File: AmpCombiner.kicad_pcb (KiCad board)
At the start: 2 copper layers, 64.1 x 34.3 mm, 22 parts, among them J1 AudioJack4, J2 AudioJack4, J3 AudioJack4, SW1 SW_SPDT, U1 TDA1517

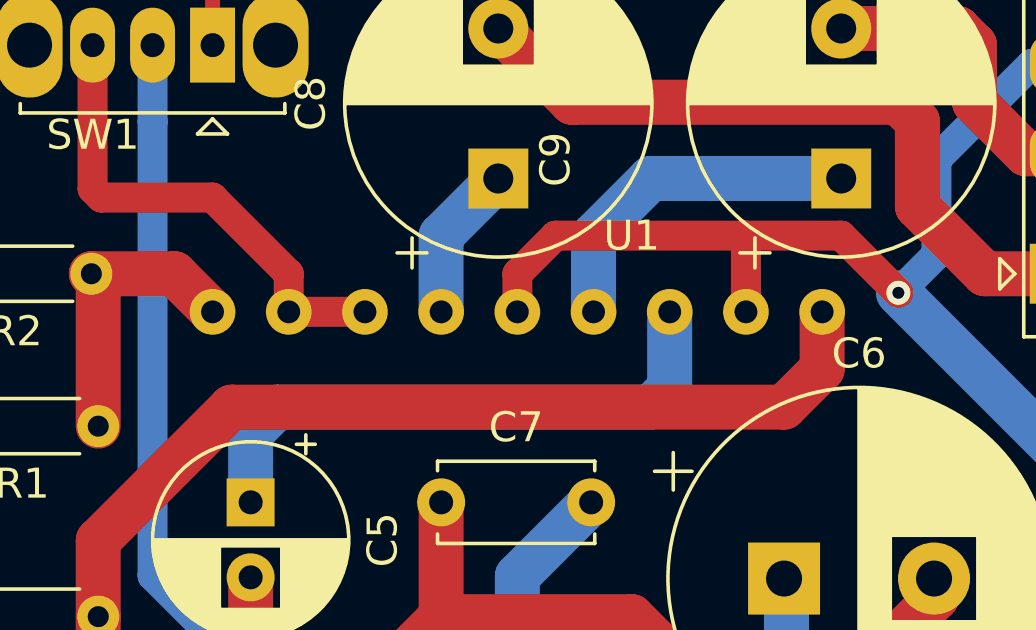
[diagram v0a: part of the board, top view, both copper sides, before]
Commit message: Update docs, standard footprint
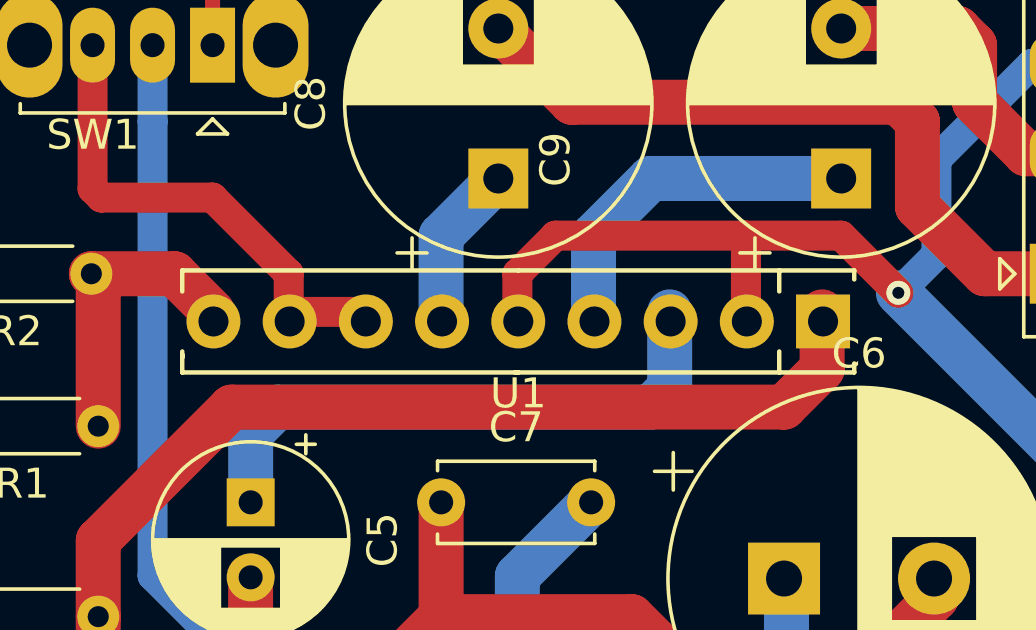
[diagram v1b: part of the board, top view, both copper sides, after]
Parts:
- U1: footprint KiLib:SOT110-1 -> Package_SIP:SIP9_Housing
- moved U1 7.81 mm to (172.8, 107.0)
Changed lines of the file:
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@@
   (general
     (thickness 1.6)
-    (drawings 5)
+    (drawings 7)
     (tracks 120)
     (zones 0)
@@
     (add_net "Net-(R3-Pad1)")
     (add_net "Net-(SW1-Pad3)")
+  )
+  (module Package_SIP:SIP9_Housing (layer F.Cu)
+    (at 172.75 107 180)
+    (descr SIP9)
+    (tags SIP9)
+    (fp_text reference U1 (at 10.16 -2.4) (layer F.SilkS)
+      (effects (font (size 1 1) (thickness 0.15)))
+    )
+    (fp_text value TDA1517 (at 10.16 2.5) (layer F.Fab)
+      (effects (font (size 1 1) (thickness 0.15)))
+    )
+    (fp_line (start 21.56 -1.9) (end -1.24 -2) (layer F.CrtYd) (width 0.05))
+    (fp_line (start 21.56 1.9) (end 21.56 -1.9) (layer F.CrtYd) (width 0.05))
+    (fp_line (start -1.24 2) (end 21.56 1.9) (layer F.CrtYd) (width 0.05))
+    (fp_line (start -1.24 -2) (end -1.24 2) (layer F.CrtYd) (width 0.05))
+    (fp_line (start 0.06 -1.6) (end 21.26 -1.6) (layer F.Fab) (width 0.1))
+    (fp_line (start -0.94 -0.6) (end 0.06 -1.6) (layer F.Fab) (width 0.1))
+    (fp_line (start -0.94 1.6) (end -0.94 -0.6) (layer F.Fab) (width 0.1))
+    (fp_line (start 21.26 1.6) (end -0.94 1.6) (layer F.Fab) (width 0.1))
+    (fp_line (start 21.26 -1.6) (end 21.26 1.6) (layer F.Fab) (width 0.1))
+    (fp_line (start 21.36 -1.7) (end 21.36 -1.1) (layer F.SilkS) (width 0.15))
+    (fp_line (start 10.16 -1.7) (end 21.36 -1.7) (layer F.SilkS) (width 0.15))
+    (fp_line (start -1.04 -1.7) (end -1.04 -1.4) (layer F.SilkS) (width 0.15))
+    (fp_line (start 10.26 -1.7) (end -1.04 -1.7) (layer F.SilkS) (width 0.15))
+    (fp_line (start 21.36 1.7) (end 21.36 1) (layer F.SilkS) (width 0.15))
+    (fp_line (start 10.16 1.7) (end 21.36 1.7) (layer F.SilkS) (width 0.15))
+    (fp_line (start 21.36 -1.2) (end 21.36 -1) (layer F.SilkS) (width 0.15))
+    (fp_line (start -1.04 1.7) (end -1.04 1.4) (layer F.SilkS) (width 0.15))
+    (fp_line (start 10.16 1.7) (end -1.04 1.7) (layer F.SilkS) (width 0.15))
+    (fp_line (start 1.46 -1.7) (end 1.46 -1) (layer F.SilkS) (width 0.15))
+    (fp_line (start 1.46 1.7) (end 1.46 1) (layer F.SilkS) (width 0.15))
+    (fp_text user %R (at 10.16 0) (layer F.Fab)
+      (effects (font (size 1 1) (thickness 0.15)))
+    )
+    (pad 9 thru_hole circle (at 20.32 0 270) (size 1.8 1.8) (drill 1) (layers *.Cu *.Mask)
+      (net 18 "Net-(R1-Pad1)"))
+    (pad 8 thru_hole circle (at 17.78 0 270) (size 1.8 1.8) (drill 1) (layers *.Cu *.Mask)
+      (net 20 "Net-(SW1-Pad3)"))
+    (pad 7 thru_hole circle (at 15.24 0 270) (size 1.8 1.8) (drill 1) (layers *.Cu *.Mask)
+      (net 20 "Net-(SW1-Pad3)"))
+    (pad 6 thru_hole circle (at 12.7 0 270) (size 1.8 1.8) (drill 1) (layers *.Cu *.Mask)
+      (net 13 "Net-(C8-Pad1)"))
+    (pad 5 thru_hole circle (at 10.16 0 270) (size 1.8 1.8) (drill 1) (layers *.Cu *.Mask)
+      (net 9 GND))
+    (pad 4 thru_hole circle (at 7.62 0 270) (size 1.8 1.8) (drill 1) (layers *.Cu *.Mask)
+      (net 15 "Net-(C9-Pad1)"))
+    (pad 3 thru_hole circle (at 5.08 0 270) (size 1.8 1.8) (drill 1) (layers *.Cu *.Mask)
+      (net 10 "Net-(C5-Pad1)"))
+    (pad 2 thru_hole circle (at 2.54 0 270) (size 1.8 1.8) (drill 1) (layers *.Cu *.Mask)
+      (net 9 GND))
+    (pad 1 thru_hole rect (at 0 0 270) (size 1.8 1.8) (drill 1) (layers *.Cu *.Mask)
+      (net 19 "Net-(R3-Pad1)"))
+    (model ${KISYS3DMOD}/Package_SIP.3dshapes/SIP9_Housing.wrl
+      (at (xyz 0 0 0))
+      (scale (xyz 1 1 1))
+      (rotate (xyz 0 0 0))
+    )
   )
   (module Capacitor_THT:CP_Radial_D6.3mm_P2.50mm (layer F.Cu)
@@
       (net 11 +9V))
   )
-  (module KiLib:SOT110-1 (layer F.Cu)
-    (at 165.1 105.41 180)
-    (fp_text reference U1 (at -1.27 1.27) (layer F.SilkS)
-      (effects (font (size 1 1) (thickness 0.15)))
-    )
-    (fp_text value TDA1517 (at 0 -3.175) (layer F.Fab)
-      (effects (font (size 1 1) (thickness 0.15)))
-    )
-    (fp_line (start -8.255 -2.54) (end -7.62 -2.54) (layer F.CrtYd) (width 0.12))
-    (fp_line (start -8.89 -1.905) (end -8.255 -2.54) (layer F.CrtYd) (width 0.12))
-    (fp_line (start -8.89 -0.635) (end -8.89 -1.905) (layer F.CrtYd) (width 0.12))
-    (fp_line (start -8.255 0) (end -8.89 -0.635) (layer F.CrtYd) (width 0.12))
-    (fp_line (start 13.335 0) (end -8.255 0) (layer F.CrtYd) (width 0.12))
-    (fp_line (start 13.97 -0.635) (end 13.335 0) (layer F.CrtYd) (width 0.12))
-    (fp_line (start 13.97 -1.905) (end 13.97 -0.635) (layer F.CrtYd) (width 0.12))
-    (fp_line (start 13.335 -2.54) (end 13.97 -1.905) (layer F.CrtYd) (width 0.12))
-    (fp_line (start 12.7 -2.54) (end 13.335 -2.54) (layer F.CrtYd) (width 0.12))
-    (fp_line (start -7.62 -2.54) (end 12.7 -2.54) (layer F.CrtYd) (width 0.12))
-    (pad 9 thru_hole circle (at 12.7 -1.27 180) (size 1.524 1.524) (drill 0.762) (layers *.Cu *.Mask)
-      (net 18 "Net-(R1-Pad1)"))
-    (pad 8 thru_hole circle (at 10.16 -1.27 180) (size 1.524 1.524) (drill 0.762) (layers *.Cu *.Mask)
-      (net 20 "Net-(SW1-Pad3)"))
-    (pad 7 thru_hole circle (at 7.62 -1.27 180) (size 1.524 1.524) (drill 0.762) (layers *.Cu *.Mask)
-      (net 20 "Net-(SW1-Pad3)"))
-    (pad 6 thru_hole circle (at 5.08 -1.27 180) (size 1.524 1.524) (drill 0.762) (layers *.Cu *.Mask)
-      (net 13 "Net-(C8-Pad1)"))
-    (pad 5 thru_hole circle (at 2.54 -1.27 180) (size 1.524 1.524) (drill 0.762) (layers *.Cu *.Mask)
-      (net 9 GND))
-    (pad 4 thru_hole circle (at 0 -1.27 180) (size 1.524 1.524) (drill 0.762) (layers *.Cu *.Mask)
-      (net 15 "Net-(C9-Pad1)"))
-    (pad 3 thru_hole circle (at -2.54 -1.27 180) (size 1.524 1.524) (drill 0.762) (layers *.Cu *.Mask)
-      (net 10 "Net-(C5-Pad1)"))
-    (pad 2 thru_hole circle (at -5.08 -1.27 180) (size 1.524 1.524) (drill 0.762) (layers *.Cu *.Mask)
-      (net 9 GND))
-    (pad 1 thru_hole circle (at -7.62 -1.27 180) (size 1.524 1.524) (drill 0.762) (layers *.Cu *.Mask)
-      (net 19 "Net-(R3-Pad1)"))
-  )
   (module Resistor_THT:R_Axial_DIN0204_L3.6mm_D1.6mm_P5.08mm_Horizontal (layer F.Cu)
     (at 135.89 95.885)
@@
     )
   )
+  (dimension 34.29 (width 0.12) (layer Dwgs.User)
+    (gr_text "34.290 mm" (at 192.77 111.125 90) (layer Dwgs.User)
+      (effects (font (size 1 1) (thickness 0.15)))
+    )
+    (feature1 (pts (xy 187.96 93.98) (xy 192.086421 93.98)))
+    (feature2 (pts (xy 187.96 128.27) (xy 192.086421 128.27)))
+    (crossbar (pts (xy 191.5 128.27) (xy 191.5 93.98)))
+    (arrow1a (pts (xy 191.5 93.98) (xy 192.086421 95.106504)))
+    (arrow1b (pts (xy 191.5 93.98) (xy 190.913579 95.106504)))
+    (arrow2a (pts (xy 191.5 128.27) (xy 192.086421 127.143496)))
+    (arrow2b (pts (xy 191.5 128.27) (xy 190.913579 127.143496)))
+  )
+  (dimension 64.135 (width 0.12) (layer Dwgs.User)
+    (gr_text "64.135 mm" (at 155.8925 133.27) (layer Dwgs.User)
+      (effects (font (size 1 1) (thickness 0.15)))
+    )
+    (feature1 (pts (xy 123.825 128.27) (xy 123.825 132.586421)))
+    (feature2 (pts (xy 187.96 128.27) (xy 187.96 132.586421)))
+    (crossbar (pts (xy 187.96 132) (xy 123.825 132)))
+    (arrow1a (pts (xy 123.825 132) (xy 124.951504 131.413579)))
+    (arrow1b (pts (xy 123.825 132) (xy 124.951504 132.586421)))
+    (arrow2a (pts (xy 187.96 132) (xy 186.833496 131.413579)))
+    (arrow2b (pts (xy 187.96 132) (xy 186.833496 132.586421)))
+  )
   (gr_text "2019 (c) DevDroplets.ga" (at 180.34 120.65 45) (layer F.Cu)
